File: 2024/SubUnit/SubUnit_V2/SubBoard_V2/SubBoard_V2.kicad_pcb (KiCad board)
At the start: 2 copper layers, 66.8 x 58 mm, 30 parts, among them J1 Conn_01x02_Socket, J10 Conn_01x02_Socket, J11 Conn_01x03_Socket, J12 Conn_01x02_Socket, J13 Conn_01x02_Socket, J14 Conn_01x05_Socket, J15 Conn_01x05_Socket, J16 Conn_01x02_Socket, J18 Conn_01x07_Socket, J19 Conn_01x07_Socket, J2 Conn_01x02_Socket, J3 Conn_01x02_Socket, J4 Conn_01x02_Socket, J5 Conn_01x02_Socket, J6 Conn_01x02_Socket, J7 Conn_01x02_Socket, J8 Conn_01x02_Socket, J9 Conn_01x02_Socket

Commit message: 軽微な修正とフットプリントライブラリの追加
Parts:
- added ?: , , F.Cu at (-11.8, 22.4)
- added ?: , , F.Cu at (14.1, -4.83)
- added ?: , , F.Cu at (11.4, 22.2)
- added REF**: MountingHole_2.2mm_M2_DIN965_Pad, MountingHole:MountingHole_2.2mm_M2_DIN965_Pad, F.Cu at (-14.0, -5.00)
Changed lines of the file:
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@@
     )
   )
+  (footprint "" (layer "F.Cu")
+    (at -11.811 22.352)
+    (fp_text reference "" (at 0 0) (layer "F.SilkS")
+        (effects (font (size 1.27 1.27) (thickness 0.15)))
+    )
+    (fp_text value "" (at 0 0) (layer "F.SilkS")
+        (effects (font (size 1.27 1.27) (thickness 0.15)))
+    )
+    (pad "1" thru_hole circle (at 0.303 -0.098) (size 3.8 3.8) (drill 2.2) (layers "*.Cu" "*.Mask"))
+  )
   (footprint "Capacitor_THT:CP_Radial_D10.0mm_P5.00mm" locked (layer "F.Cu")
     (at 6 -4 -90)
@@
     )
   )
+  (footprint "" (layer "F.Cu")
+    (at 14.097 -4.826)
+    (fp_text reference "" (at 0 0) (layer "F.SilkS")
+        (effects (font (size 1.27 1.27) (thickness 0.15)))
+    )
+    (fp_text value "" (at 0 0) (layer "F.SilkS")
+        (effects (font (size 1.27 1.27) (thickness 0.15)))
+    )
+    (pad "1" thru_hole circle (at -0.097 -0.174) (size 3.8 3.8) (drill 2.2) (layers "*.Cu" "*.Mask"))
+  )
   (footprint "Connector_Molex:Molex_SPOX_5267-05A_1x05_P2.50mm_Vertical" locked (layer "F.Cu")
     (at -5 20)
@@
     )
   )
+  (footprint "MountingHole:MountingHole_2.2mm_M2_DIN965_Pad" (layer "F.Cu")
+    (at -14 -5)
+    (descr "Mounting Hole 2.2mm, M2, DIN965")
+    (tags "mounting hole 2.2mm m2 din965")
+    (attr exclude_from_pos_files exclude_from_bom)
+    (fp_text reference "REF**" (at 0 -2.9) (layer "F.SilkS")
+        (effects (font (size 1 1) (thickness 0.15)))
+    )
+    (fp_text value "MountingHole_2.2mm_M2_DIN965_Pad" (at 0 2.9) (layer "F.Fab")
+        (effects (font (size 1 1) (thickness 0.15)))
+    )
+    (fp_text user "${REFERENCE}" (at 0 0) (layer "F.Fab")
+        (effects (font (size 1 1) (thickness 0.15)))
+    )
+    (fp_circle (center 0 0) (end 1.9 0)
+      (stroke (width 0.15) (type solid)) (fill none) (layer "Cmts.User"))
+    (fp_circle (center 0 0) (end 2.15 0)
+      (stroke (width 0.05) (type solid)) (fill none) (layer "F.CrtYd"))
+    (pad "1" thru_hole circle (at 0 0) (size 3.8 3.8) (drill 2.2) (layers "*.Cu" "*.Mask"))
+  )
   (footprint "Resistor_SMD:R_0603_1608Metric" (layer "F.Cu")
     (at -15.494 -18.669 90)
@@
     )
   )
+  (footprint "" (layer "F.Cu")
+    (at 11.43 22.225)
+    (fp_text reference "" (at 0 0) (layer "F.SilkS")
+        (effects (font (size 1.27 1.27) (thickness 0.15)))
+    )
+    (fp_text value "" (at 0 0) (layer "F.SilkS")
+        (effects (font (size 1.27 1.27) (thickness 0.15)))
+    )
+    (pad "1" thru_hole circle (at 0 0) (size 3.8 3.8) (drill 2.2) (layers "*.Cu" "*.Mask"))
+  )
   (footprint "Resistor_SMD:R_0603_1608Metric" (layer "F.Cu")
     (at 13.97 -16.002)
@@
   )
   (footprint "Connector_PinHeader_2.54mm:PinHeader_1x07_P2.54mm_Vertical" locked (layer "B.Cu")
-    (at -7.6 27 -90)
+    (at -7.56 27 -90)
     (descr "Through hole straight pin header, 1x07, 2.54mm pitch, single row")
     (tags "Through hole pin header THT 1x07 2.54mm single row")
@@
     (effects (font (size 0.8 0.8) (thickness 0.1) italic) (justify left bottom mirror))
   )
-  (segment (start -19.05 18.542) (end -19.05 15.147056) (width 0.25) (layer "F.Cu") (net 2))
-  (segment (start -19.05 15.147056) (end -22 12.197056) (width 0.25) (layer "F.Cu") (net 2))
   (segment (start 5 19.812) (end 4.125 18.937) (width 0.25) (layer "F.Cu") (net 2))
   (segment (start 18.322 18) (end 28.5 7.822) (width 0.25) (layer "F.Cu") (net 2))
   (segment (start 5 19.812) (end 5 19.892) (width 0.25) (layer "F.Cu") (net 2))
+  (segment (start -22 12.197056) (end -22 10.5) (width 0.25) (layer "F.Cu") (net 2))
   (segment (start 14.5 18) (end 18.322 18) (width 0.25) (layer "F.Cu") (net 2))
-  (segment (start -8.948 28.644) (end -19.05 18.542) (width 0.25) (layer "F.Cu") (net 2))
+  (segment (start -19.05 15.147056) (end -22 12.197056) (width 0.25) (layer "F.Cu") (net 2))
   (segment (start -30.75 1.225) (end -24.525 -5) (width 0.25) (layer "F.Cu") (net 2))
   (segment (start 4.125 18.937) (end 4.125 15.4) (width 0.25) (layer "F.Cu") (net 2))
   (segment (start 5.75 13.25) (end 10.55 13.25) (width 0.25) (layer "F.Cu") (net 2))
+  (segment (start -8.948 28.644) (end -19.05 18.542) (width 0.25) (layer "F.Cu") (net 2))
   (segment (start -22 10.5) (end -24.2 8.3) (width 0.25) (layer "F.Cu") (net 2))
   (segment (start 10.55 13.25) (end 14.5 17.2) (width 0.25) (layer "F.Cu") (net 2))
   (segment (start 4.125 15.4) (end 4.125 14.875) (width 0.25) (layer "F.Cu") (net 2))
+  (segment (start 3.81 21.336) (end 3.81 25.79) (width 0.25) (layer "F.Cu") (net 2))
   (segment (start -28.35 8.3) (end -30.75 5.9) (width 0.25) (layer "F.Cu") (net 2))
-  (segment (start -22 12.197056) (end -22 10.5) (width 0.25) (layer "F.Cu") (net 2))
   (segment (start 5 14) (end 5.75 13.25) (width 0.25) (layer "F.Cu") (net 2))
-  (segment (start 5 20.146) (end 3.81 21.336) (width 0.25) (layer "F.Cu") (net 2))
-  (segment (start 0.966 28.644) (end -8.948 28.644) (width 0.25) (layer "F.Cu") (net 2))
-  (segment (start 5 19.812) (end 5 20.146) (width 0.25) (layer "F.Cu") (net 2))
+  (segment (start 0.956 28.644) (end -8.948 28.644) (width 0.25) (layer "F.Cu") (net 2))
   (segment (start -24.525 -5) (end -22.5 -5) (width 0.25) (layer "F.Cu") (net 2))
+  (segment (start 5 20.146) (end 3.81 21.336) (width 0.25) (layer "F.Cu") (net 2))
   (segment (start 14.5 17.2) (end 14.5 18) (width 0.25) (layer "F.Cu") (net 2))
-  (segment (start 3.81 25.8) (end 0.966 28.644) (width 0.25) (layer "F.Cu") (net 2))
+  (segment (start 5 19.812) (end 5 20.146) (width 0.25) (layer "F.Cu") (net 2))
+  (segment (start 3.81 25.79) (end 2.6 27) (width 0.25) (layer "F.Cu") (net 2))
+  (segment (start 0.956 28.644) (end 2.6 27) (width 0.25) (layer "F.Cu") (net 2))
   (segment (start -30.75 5.9) (end -30.75 1.225) (width 0.25) (layer "F.Cu") (net 2))
   (segment (start -24.2 8.3) (end -28.35 8.3) (width 0.25) (layer "F.Cu") (net 2))
   (segment (start 4.125 14.875) (end 5 14) (width 0.25) (layer "F.Cu") (net 2))
-  (segment (start 3.81 21.336) (end 3.81 25.8) (width 0.25) (layer "F.Cu") (net 2))
+  (segment (start -19.05 18.542) (end -19.05 15.147056) (width 0.25) (layer "F.Cu") (net 2))
   (segment (start 28.5 7.822) (end 28.5 3.5) (width 0.25) (layer "F.Cu") (net 2))
   (segment (start 14.710786 16.585786) (end 15.914214 16.585786) (width 0.25) (layer "F.Cu") (net 3))
@@
   (segment (start -30.275 5.625) (end -28.075 7.825) (width 0.25) (layer "F.Cu") (net 3))
   (segment (start 1.385 25.215) (end 1.385 27.3467) (width 0.25) (layer "F.Cu") (net 3))
-  (segment (start -19 -11) (end -19 -10.874) (width 0.25) (layer "B.Cu") (net 4))
-  (segment (start -8.716976 28.194) (end -3.664 28.194) (width 0.25) (layer "B.Cu") (net 4))
-  (segment (start -30.004696 6.90628) (end -8.716976 28.194) (width 0.25) (layer "B.Cu") (net 4))
-  (segment (start -19 -10.874) (end -30.004696 0.130696) (width 0.25) (layer "B.Cu") (net 4))
-  (segment (start -3.664 28.194) (end -2.47 27) (width 0.25) (layer "B.Cu") (net 4))
   (segment (start -30.004696 0.130696) (end -30.004696 6.90628) (width 0.25) (layer "B.Cu") (net 4))
+  (segment (start -19 -10.874) (end -30.004696 0.130696) (width 0.25) (layer "B.Cu") (net 4))
+  (segment (start -2.48 27) (end -2.47 27) (width 0.25) (layer "B.Cu") (net 4))
+  (segment (start -30.004696 6.90628) (end -8.716976 28.194) (width 0.25) (layer "B.Cu") (net 4))
+  (segment (start -3.674 28.194) (end -2.48 27) (width 0.25) (layer "B.Cu") (net 4))
+  (segment (start -8.716976 28.194) (end -3.674 28.194) (width 0.25) (layer "B.Cu") (net 4))
+  (segment (start -19 -11) (end -19 -10.874) (width 0.25) (layer "B.Cu") (net 4))
   (segment (start -15.494 -19.994) (end -18 -22.5) (width 0.25) (layer "F.Cu") (net 5))
   (segment (start -15.494 -19.494) (end -15.494 -19.994) (width 0.25) (layer "F.Cu") (net 5))
-  (segment (start -8.903372 28.644) (end -1.574 28.644) (width 0.25) (layer "B.Cu") (net 5))
+  (segment (start 0.06 27) (end 0.07 27) (width 0.25) (layer "B.Cu") (net 5))
+  (segment (start -1.584 28.644) (end 0.06 27) (width 0.25) (layer "B.Cu") (net 5))
+  (segment (start -8.903372 28.644) (end -1.584 28.644) (width 0.25) (layer "B.Cu") (net 5))
+  (segment (start -30.48 7.067372) (end -8.903372 28.644) (width 0.25) (layer "B.Cu") (net 5))
   (segment (start -20.32 -20.18) (end -20.32 -10.190396) (width 0.25) (layer "B.Cu") (net 5))
   (segment (start -20.32 -10.190396) (end -30.48 -0.030396) (width 0.25) (layer "B.Cu") (net 5))
   (segment (start -30.48 -0.030396) (end -30.48 7.067372) (width 0.25) (layer "B.Cu") (net 5))
-  (segment (start -1.574 28.644) (end 0.07 27) (width 0.25) (layer "B.Cu") (net 5))
-  (segment (start -30.48 7.067372) (end -8.903372 28.644) (width 0.25) (layer "B.Cu") (net 5))
   (segment (start -18 -22.5) (end -20.32 -20.18) (width 0.25) (layer "B.Cu") (net 5))
   (segment (start 14.795 -19.676497) (end 17.618503 -22.5) (width 0.3) (layer "F.Cu") (net 6))

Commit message: あとシルクとDRC通すだけ
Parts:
- removed ? (x3): , 
- removed D3: NeoPixel_THT, LED_SMD:LED_Inolux_IN-PI554FCH_PLCC4_5.0x5.0mm_P3.2mm
- removed R5: 100, Resistor_SMD:R_0603_1608Metric
- removed REF**: MountingHole_2.2mm_M2_DIN965_Pad, MountingHole:MountingHole_2.2mm_M2_DIN965_Pad
- moved D2 3.81 mm to (18.3, -15.7)
- moved R3 3.56 mm to (18.3, -11.7)
- moved D1 3.56 mm to (18.3, -13.7)
- moved R4 2.03 mm to (14.0, -15.7)
- moved R1 2.03 mm to (14.0, -17.5)
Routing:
- net NEO_SIG: track 65.0 -> 0.00 mm
- net Net-(D3-VDD): track 4.40 -> 0.00 mm
- net Net-(J13-Pin_1): track 4.49 -> 6.53 mm
- net Net-(D2-A): track 3.47 -> 2.71 mm
- net GNDPWR: track 15.2 -> 14.6 mm, vias 0 -> 1

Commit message: 完成
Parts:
- removed the C1 at (-6.00, -4.00)
- added ?: , , F.Cu at (14.0, -5.00)
- added ?: , , F.Cu at (11.6, 22.6)
- added ?: , , F.Cu at (-11.4, 22.6)
- added ?: , , F.Cu at (-14.0, -5.00)
- added C4: 1000u, Capacitor_THT:CP_Radial_D10.0mm_P5.00mm, F.Cu at (-6.00, -4.00)
- added G***: LOGO, KotaroOCHIISHI:rione22, F.Cu at (-14.5, -13.2)
- added G***: LOGO, KotaroOCHIISHI:qr11, B.Cu at (17.3, -16.5)
- added G***: LOGO, KotaroOCHIISHI:rione12, B.Cu at (0.00, 8.00)
- added G***: LOGO, KotaroOCHIISHI:black, B.Cu at (-24.0, -34.0)
- added G***: LOGO, KotaroOCHIISHI:black, B.Cu at (24.0, -34.0)
- C1, C2, C3: value 1500u -> 1000u
- moved R2 3.55 mm to (-18.9, -19.8), turned to 0 degrees
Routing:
- net +15V: track 0.00 -> 11.9 mm
- net TR_SIGNAL: track 78.9 -> 77.6 mm
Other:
- board text added: "GND +BATT +6.5V CANH CANL"
- board text added: "LED"
- board text added: "PHOTO"
- board text added: "github.com /Rione /ssl-Circuit"

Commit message: もう発注できる
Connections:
- J10 pad 1: +15V -> GNDPWR
- J10 pad 2: GNDPWR -> +15V
- J9 pad 1: +15V -> GNDPWR
- J9 pad 2: GNDPWR -> +15V
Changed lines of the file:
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@@
       (stroke (width 0.1) (type solid)) (layer "F.Fab"))
     (pad "1" thru_hole rect locked (at 0 0 225) (size 3 3) (drill 1.8) (layers "*.Cu" "*.Mask")
-      (net 1 "+15V") (pinfunction "Pin_1") (pintype "passive"))
+      (net 7 "GNDPWR") (pinfunction "Pin_1") (pintype "passive"))
     (pad "2" thru_hole circle locked (at 5 0 225) (size 3 3) (drill 1.8) (layers "*.Cu" "*.Mask")
-      (net 7 "GNDPWR") (pinfunction "Pin_2") (pintype "passive"))
+      (net 1 "+15V") (pinfunction "Pin_2") (pintype "passive"))
     (model "${KICAD6_3DMODEL_DIR}/Connector_AMASS.3dshapes/AMASS_XT30UPB-M_1x02_P5.0mm_Vertical.wrl"
       (offset (xyz 0 0 0))
@@
       (stroke (width 0.1) (type solid)) (layer "F.Fab"))
     (pad "1" thru_hole rect locked (at 0 0 315) (size 3 3) (drill 1.8) (layers "*.Cu" "*.Mask")
-      (net 1 "+15V") (pinfunction "Pin_1") (pintype "passive"))
+      (net 7 "GNDPWR") (pinfunction "Pin_1") (pintype "passive"))
     (pad "2" thru_hole circle locked (at 5 0 315) (size 3 3) (drill 1.8) (layers "*.Cu" "*.Mask")
-      (net 7 "GNDPWR") (pinfunction "Pin_2") (pintype "passive"))
+      (net 1 "+15V") (pinfunction "Pin_2") (pintype "passive"))
     (model "${KICAD6_3DMODEL_DIR}/Connector_AMASS.3dshapes/AMASS_XT30UPB-M_1x02_P5.0mm_Vertical.wrl"
       (offset (xyz 0 0 0))

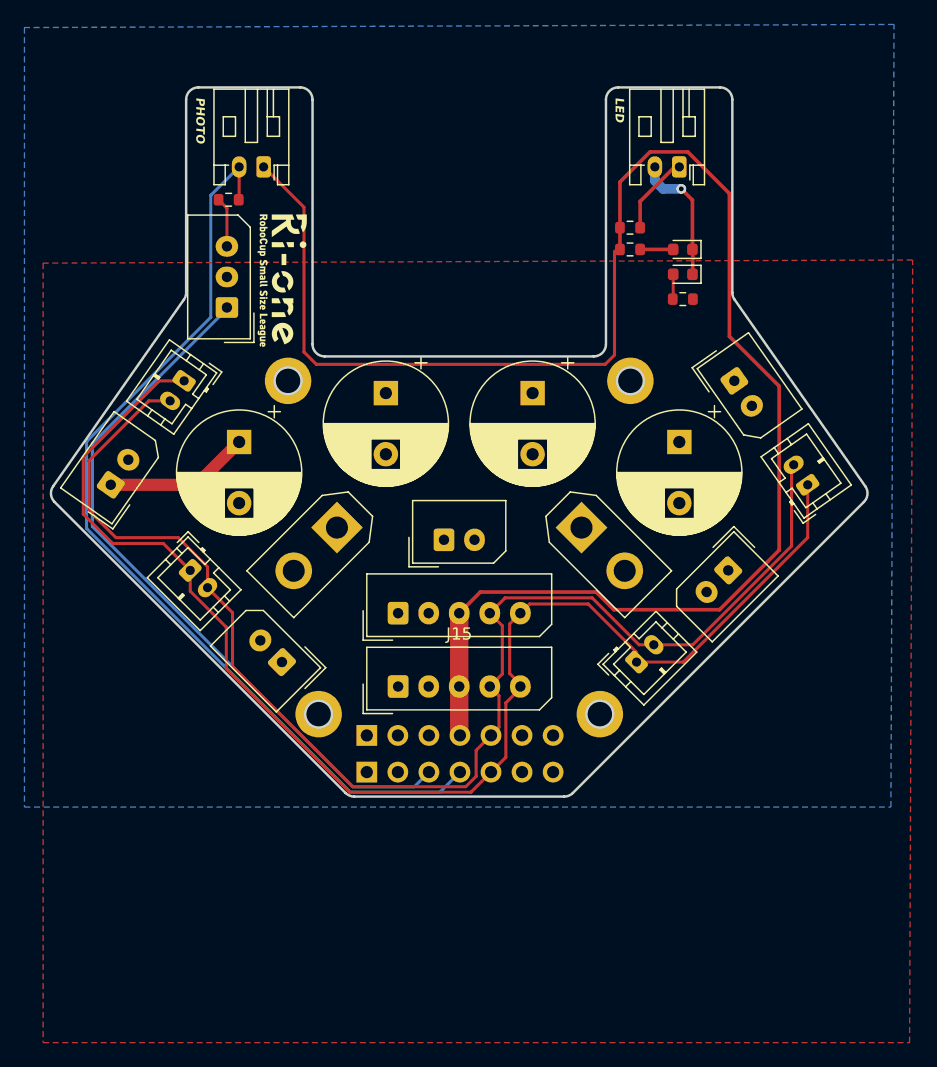
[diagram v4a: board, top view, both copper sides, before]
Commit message: hvsの干渉を直した
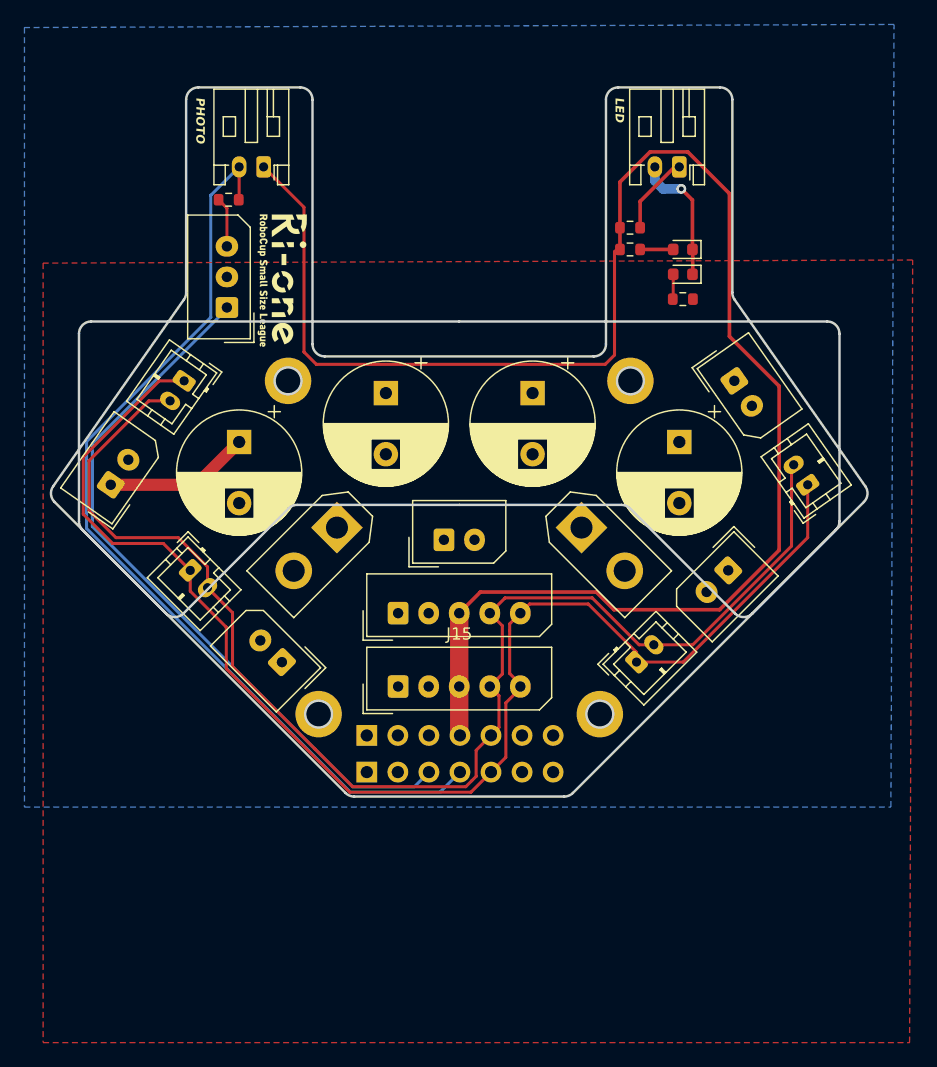
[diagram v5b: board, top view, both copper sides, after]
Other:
- outline, holes or cut-outs redrawn
